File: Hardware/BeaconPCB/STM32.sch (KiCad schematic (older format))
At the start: 11 parts

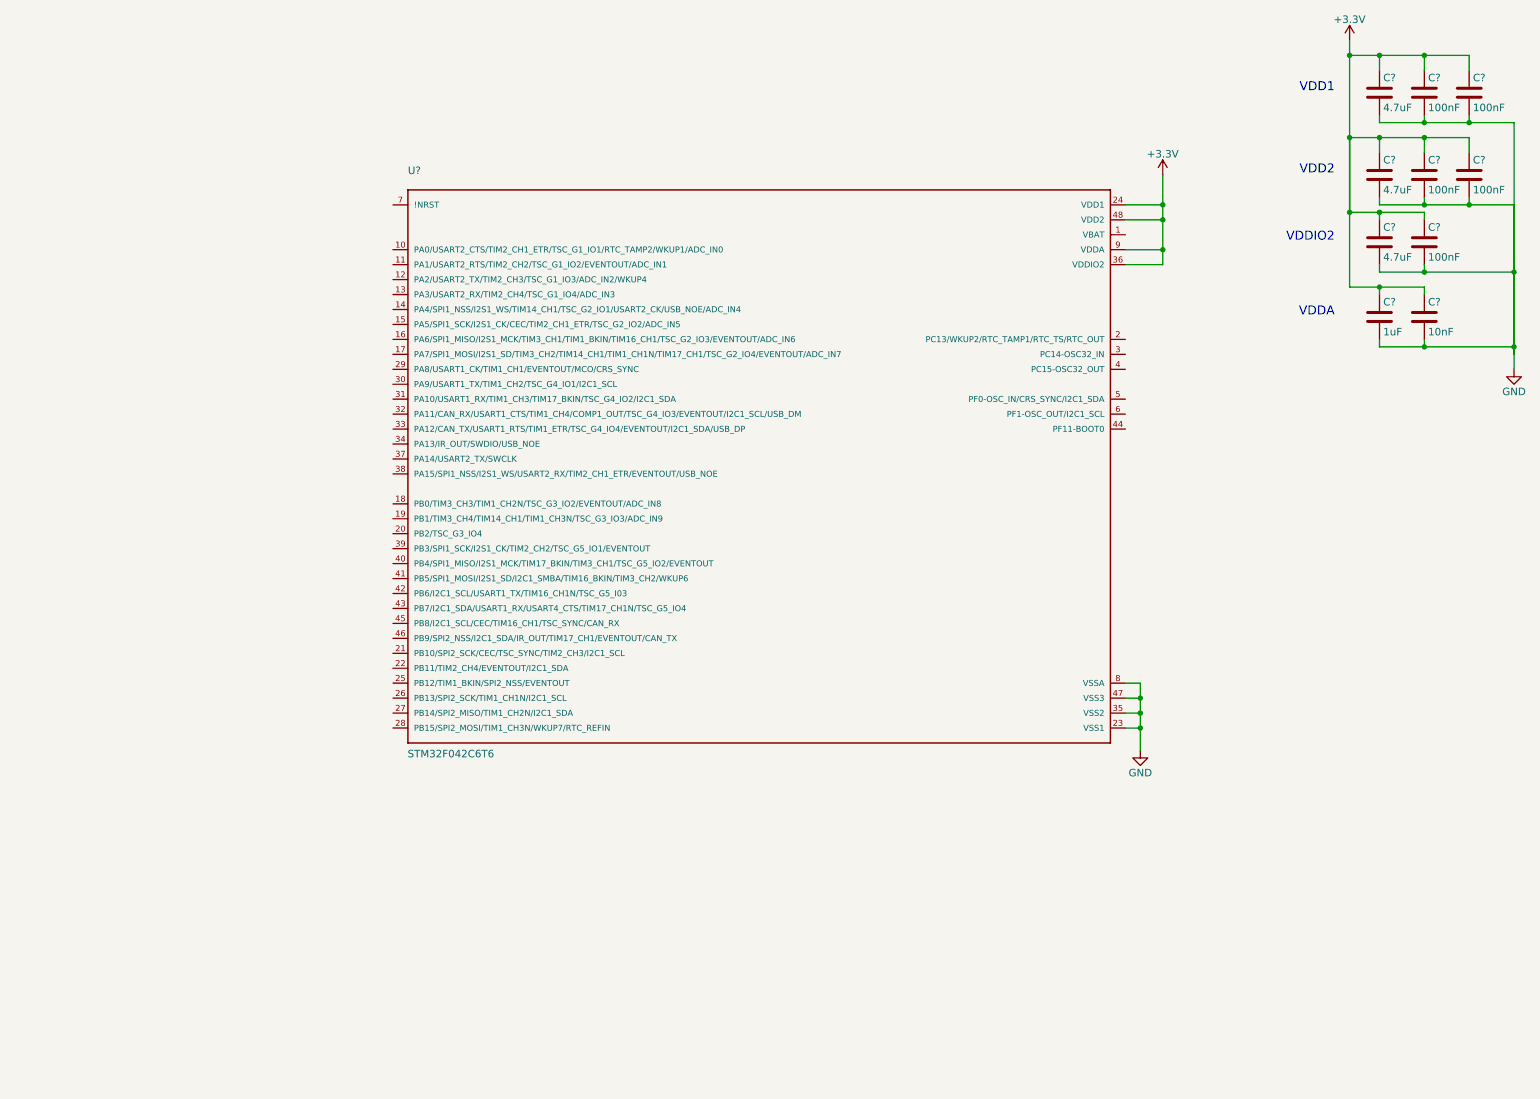
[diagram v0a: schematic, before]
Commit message: Base STM32 circuit schematic done
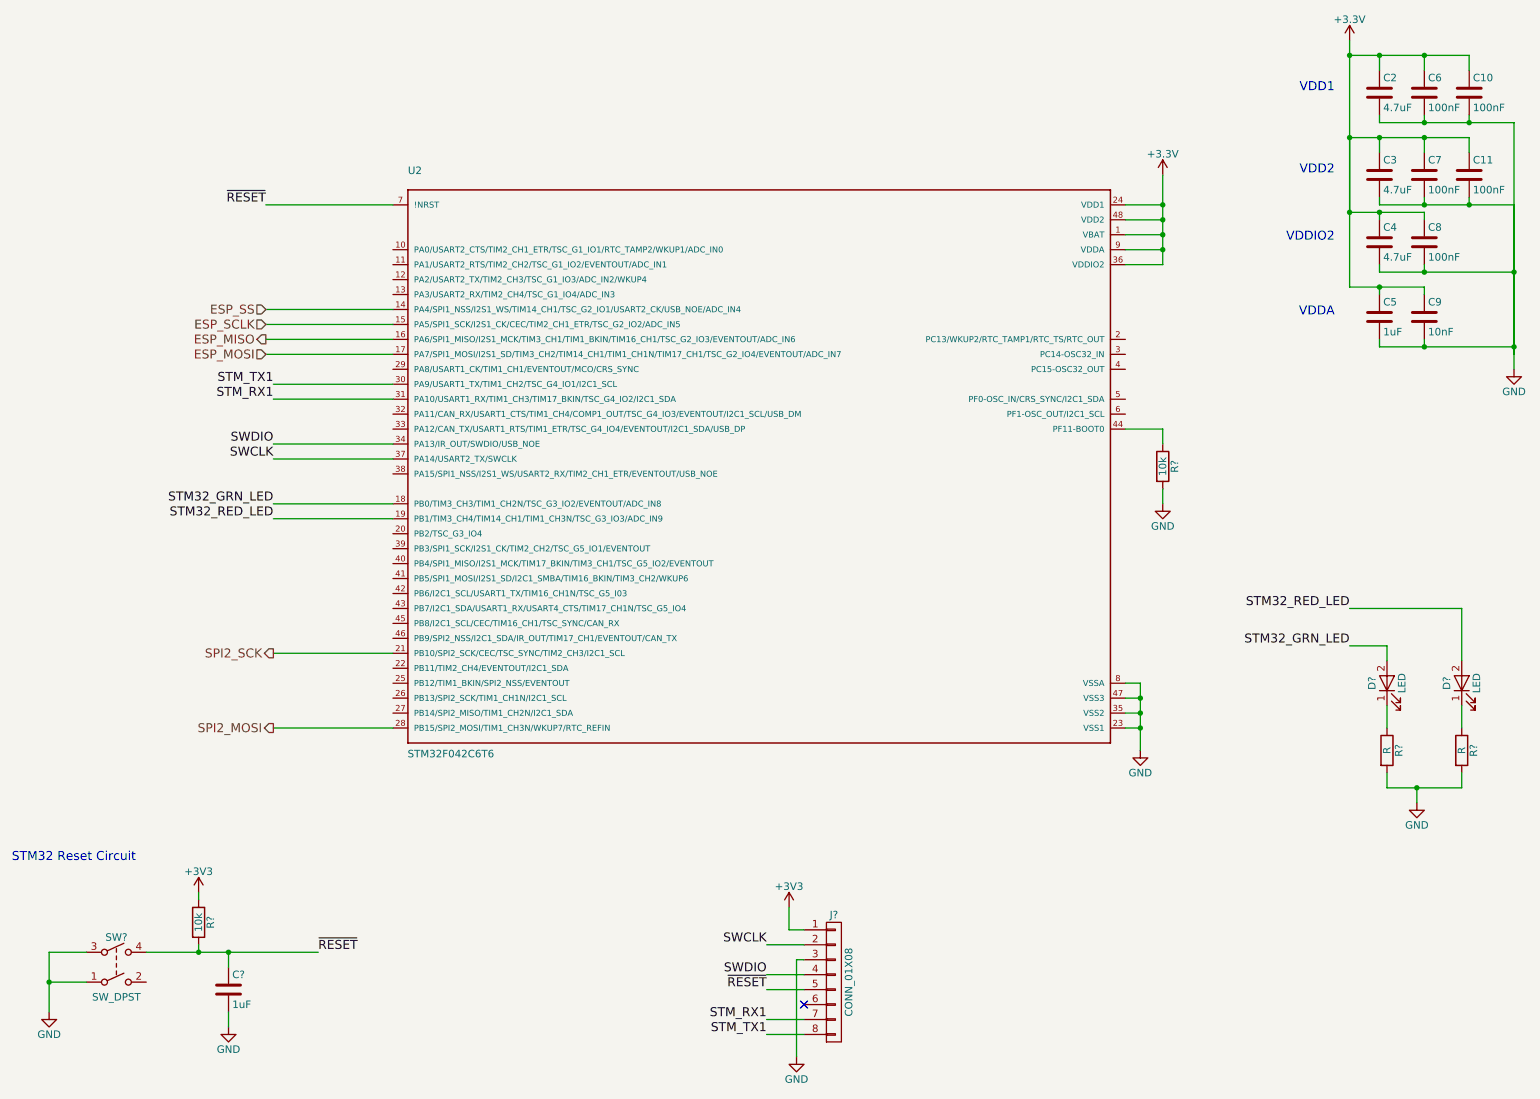
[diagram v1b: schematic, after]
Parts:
- added C?: 1uF, symbol C
- added D? (x2): LED, symbol LED
- added J?: CONN_01X08, symbol CONN_01X08
- added R? (x2): 10k, symbol R
- added R? (x2): R, symbol R
- added SW?: SW_DPST, symbol SW_DPST
- gave numbers to parts that had none: 11
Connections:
- net +3V3: now also U2.1 (VBAT), J?.1 (P1), R?.1
- net GND: now also C?.2, J?.3 (P3), R?.2, R?.2, R?.2, SW?.1, SW?.3
- net ESP_SS: now reaches U2.14 (PA4/SPI1_NSS/I2S1_WS/TIM14_CH1/TSC_G2_IO1/USART2_CK/USB_NOE/ADC_IN4)
- net ESP_SCLK: now reaches U2.15 (PA5/SPI1_SCK/I2S1_CK/CEC/TIM2_CH1_ETR/TSC_G2_IO2/ADC_IN5)
- net ESP_MISO: now reaches U2.16 (PA6/SPI1_MISO/I2S1_MCK/TIM3_CH1/TIM1_BKIN/TIM16_CH1/TSC_G2_IO3/EVENTOUT/ADC_IN6)
- net ESP_MOSI: now reaches U2.17 (PA7/SPI1_MOSI/I2S1_SD/TIM3_CH2/TIM14_CH1/TIM1_CH1N/TIM17_CH1/TSC_G2_IO4/EVENTOUT/ADC_IN7)
- net STM32_GRN_LED: now reaches U2.18 (PB0/TIM3_CH3/TIM1_CH2N/TSC_G3_IO2/EVENTOUT/ADC_IN8)
- net STM32_GRN_LED: now also D?.2 (A)
- net STM32_RED_LED: now reaches U2.19 (PB1/TIM3_CH4/TIM14_CH1/TIM1_CH3N/TSC_G3_IO3/ADC_IN9)
- net STM32_RED_LED: now also D?.2 (A)
- net SPI2_SCK: now reaches U2.21 (PB10/SPI2_SCK/CEC/TSC_SYNC/TIM2_CH3/I2C1_SCL)
- net SPI2_MOSI: now reaches U2.28 (PB15/SPI2_MOSI/TIM1_CH3N/WKUP7/RTC_REFIN)
- net STM_TX1: now reaches U2.30 (PA9/USART1_TX/TIM1_CH2/TSC_G4_IO1/I2C1_SCL)
- net STM_TX1: now also J?.8 (P8)
- net STM_RX1: now reaches U2.31 (PA10/USART1_RX/TIM1_CH3/TIM17_BKIN/TSC_G4_IO2/I2C1_SDA)
- net STM_RX1: now also J?.7 (P7)
- net SWDIO: now reaches U2.34 (PA13/IR_OUT/SWDIO/USB_NOE)
- net SWDIO: now also J?.4 (P4)
- net SWCLK: now reaches U2.37 (PA14/USART2_TX/SWCLK)
- net SWCLK: now also J?.2 (P2)
- net at U2.44 (PF11-BOOT0): now also R?.1
- net ~RESET: now reaches U2.7 (!NRST)
- net ~RESET: now also C?.1, J?.5 (P5), R?.2, SW?.4
- new net: D?.1 (K), R?.1 (x2)
- no-connect marks 0 -> 1
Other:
- note added: "STM32 Reset Circuit"

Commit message: Added IO buffers and APA102
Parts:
- added C? (x2): .1uF, symbol C
- added U? (x2): 74HC244, symbol 74HC244
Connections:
- net +3V3: now also C?.1, U?.20 (VCC)
- net ESP_MISO: now also U?.14 (1Y2); no longer U2.16 (PA6/SPI1_MISO/I2S1_MCK/TIM3_CH1/TIM1_BKIN/TIM16_CH1/TSC_G2_IO3/EVENTOUT/ADC_IN6)
- net ESP_MOSI: now also U?.8 (1A3); no longer U2.17 (PA7/SPI1_MOSI/I2S1_SD/TIM3_CH2/TIM14_CH1/TIM1_CH1N/TIM17_CH1/TSC_G2_IO4/EVENTOUT/ADC_IN7)
- net ESP_SCLK: now also U?.4 (1A1); no longer U2.15 (PA5/SPI1_SCK/I2S1_CK/CEC/TIM2_CH1_ETR/TSC_G2_IO2/ADC_IN5)
- net ESP_SS: now also U?.2 (1A0); no longer U2.14 (PA4/SPI1_NSS/I2S1_WS/TIM14_CH1/TSC_G2_IO1/USART2_CK/USB_NOE/ADC_IN4)
- net GND: now also C?.2, C?.2, U?.10 (GND), U?.10 (GND)
- net SPI2_MOSI: now also U?.16 (1Y1); no longer U2.28 (PB15/SPI2_MOSI/TIM1_CH3N/WKUP7/RTC_REFIN)
- net SPI2_SCK: now also U?.18 (1Y0); no longer U2.21 (PB10/SPI2_SCK/CEC/TSC_SYNC/TIM2_CH3/I2C1_SCL)
- net PORT0: now reaches U2.39 (PB3/SPI1_SCK/I2S1_CK/TIM2_CH2/TSC_G5_IO1/EVENTOUT)
- net PORT1: now reaches U2.40 (PB4/SPI1_MISO/I2S1_MCK/TIM17_BKIN/TIM3_CH1/TSC_G5_IO2/EVENTOUT)
- net PORT2: now reaches U2.41 (PB5/SPI1_MOSI/I2S1_SD/I2C1_SMBA/TIM16_BKIN/TIM3_CH2/WKUP6)
- net PORT3: now reaches U2.42 (PB6/I2C1_SCL/USART1_TX/TIM16_CH1N/TSC_G5_I03)
- net PORT4: now reaches U2.43 (PB7/I2C1_SDA/USART1_RX/USART4_CTS/TIM17_CH1N/TSC_G5_IO4)
- net PORT5: now reaches U2.45 (PB8/I2C1_SCL/CEC/TIM16_CH1/TSC_SYNC/CAN_RX)
- new net +5V: C?.1, U?.20 (VCC)
- new net SPI2_MOSI_LV: U2.28 (PB15/SPI2_MOSI/TIM1_CH3N/WKUP7/RTC_REFIN), U?.4 (1A1)
- new net SPI2_SCK_LV: U2.21 (PB10/SPI2_SCK/CEC/TSC_SYNC/TIM2_CH3/I2C1_SCL), U?.2 (1A0)
- new net STM32_MISO: U2.16 (PA6/SPI1_MISO/I2S1_MCK/TIM3_CH1/TIM1_BKIN/TIM16_CH1/TSC_G2_IO3/EVENTOUT/ADC_IN6)
- new net STM32_MOSI: U2.17 (PA7/SPI1_MOSI/I2S1_SD/TIM3_CH2/TIM14_CH1/TIM1_CH1N/TIM17_CH1/TSC_G2_IO4/EVENTOUT/ADC_IN7)
- new net STM32_SCLK: U2.15 (PA5/SPI1_SCK/I2S1_CK/CEC/TIM2_CH1_ETR/TSC_G2_IO2/ADC_IN5), U?.16 (1Y1)
- new net STM32_SS: U2.14 (PA4/SPI1_NSS/I2S1_WS/TIM14_CH1/TSC_G2_IO1/USART2_CK/USB_NOE/ADC_IN4), U?.18 (1Y0)
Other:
- moved on the sheet: C10, C11, C2, C3, C4, C5, C6, C7, C8, C9, C?, D?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

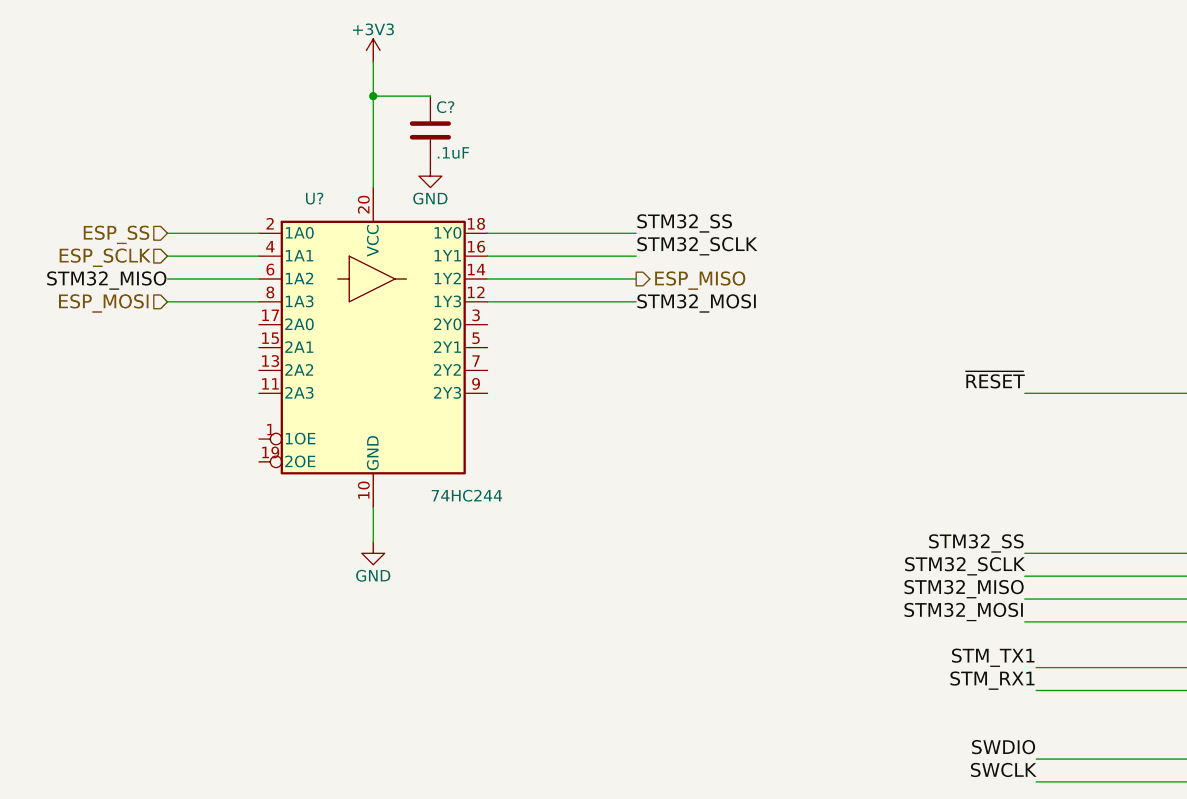
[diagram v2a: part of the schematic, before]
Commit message: Added Connectors Sheet
Started to re-arrange SPI lines
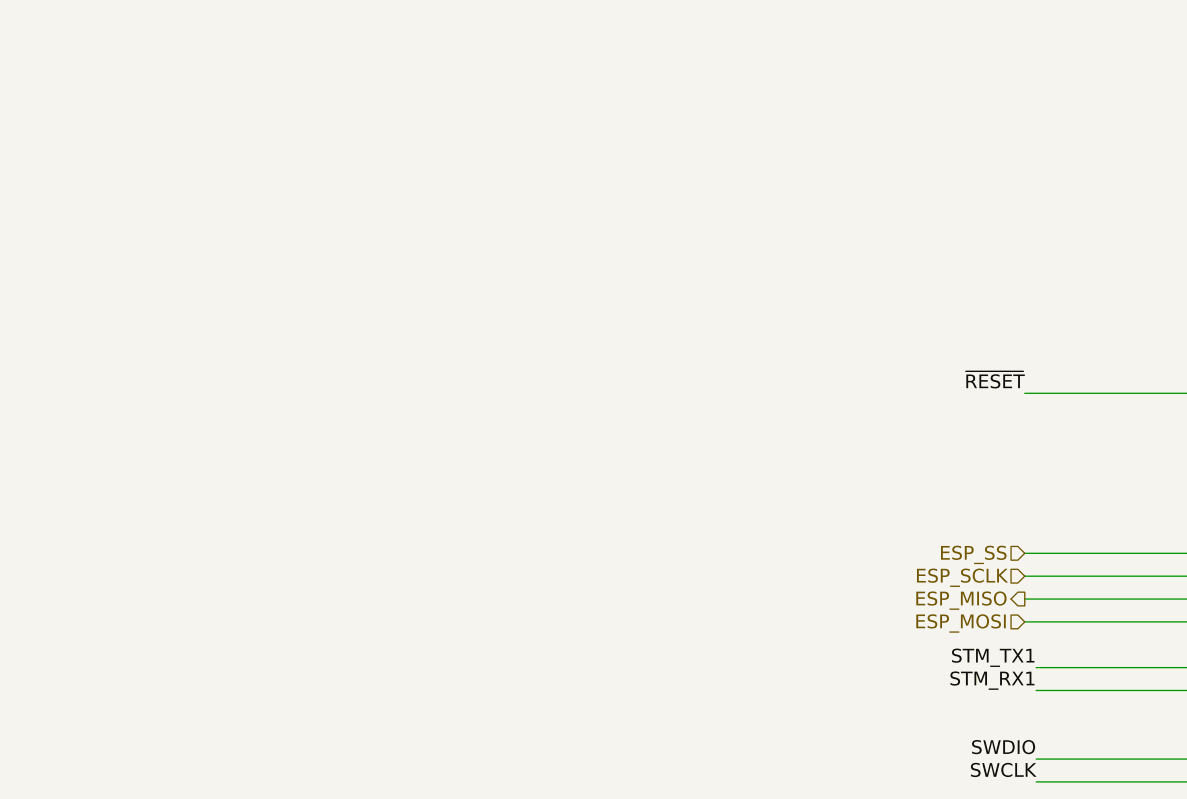
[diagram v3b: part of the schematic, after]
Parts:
- removed C?: .1uF, symbol C
- removed U?: 74HC244, symbol 74HC244
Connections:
- net STM32_MISO is gone; now on net ESP_MISO: U2.16 (PA6/SPI1_MISO/I2S1_MCK/TIM3_CH1/TIM1_BKIN/TIM16_CH1/TSC_G2_IO3/EVENTOUT/ADC_IN6)
- net STM32_MOSI is gone; now on net ESP_MOSI: U2.17 (PA7/SPI1_MOSI/I2S1_SD/TIM3_CH2/TIM14_CH1/TIM1_CH1N/TIM17_CH1/TSC_G2_IO4/EVENTOUT/ADC_IN7)
- net STM32_SCLK is gone; now on net ESP_SCLK: U2.15 (PA5/SPI1_SCK/I2S1_CK/CEC/TIM2_CH1_ETR/TSC_G2_IO2/ADC_IN5)
- net STM32_SS is gone; now on net ESP_SS: U2.14 (PA4/SPI1_NSS/I2S1_WS/TIM14_CH1/TSC_G2_IO1/USART2_CK/USB_NOE/ADC_IN4)
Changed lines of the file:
@@
 $Descr B 17000 11000
 encoding utf-8
-Sheet 3 5
+Sheet 3 6
 Title ""
 Date ""
@@
 	1    0    0    -1
 $EndComp
-Text HLabel 1800 1600 0    60   Input ~ 0
+Text HLabel 5550 3000 0    60   Input ~ 0
 ESP_SS
-Text HLabel 1800 1700 0    60   Input ~ 0
+Text HLabel 5550 3100 0    60   Input ~ 0
 ESP_SCLK
-Text HLabel 3850 1800 2    60   Output ~ 0
+Text HLabel 5550 3200 0    60   Output ~ 0
 ESP_MISO
-Text HLabel 1800 1900 0    60   Input ~ 0
+Text HLabel 5550 3300 0    60   Input ~ 0
 ESP_MOSI
 Text Label 5600 3900 2    60   ~ 0
@@
 	1    0    0    -1
 $EndComp
-$Comp
-L GND #PWR?
-U 1 1 59AECC3F
-P 2700 2950
-F 0 "#PWR?" H 2700 2700 50  0001 C CNN
-F 1 "GND" H 2700 2800 50  0000 C CNN
-F 2 "" H 2700 2950 50  0001 C CNN
-F 3 "" H 2700 2950 50  0001 C CNN
-	1    2700 2950
-	1    0    0    -1
-$EndComp
-$Comp
-L C C?
-U 1 1 59AECC45
-P 2950 1150
-F 0 "C?" H 2975 1250 50  0000 L CNN
-F 1 ".1uF" H 2975 1050 50  0000 L CNN
-F 2 "" H 2988 1000 50  0001 C CNN
-F 3 "" H 2950 1150 50  0001 C CNN
-	1    2950 1150
-	1    0    0    -1
-$EndComp
-$Comp
-L GND #PWR?
-U 1 1 59AECC4E
-P 2950 1300
-F 0 "#PWR?" H 2950 1050 50  0001 C CNN
-F 1 "GND" H 2950 1150 50  0000 C CNN
-F 2 "" H 2950 1300 50  0001 C CNN
-F 3 "" H 2950 1300 50  0001 C CNN
-	1    2950 1300
-	1    0    0    -1
-$EndComp
-$Comp
-L +3V3 #PWR?
-U 1 1 59AECCBA
-P 2700 850
-F 0 "#PWR?" H 2700 700 50  0001 C CNN
-F 1 "+3V3" H 2700 990 50  0000 C CNN
-F 2 "" H 2700 850 50  0001 C CNN
-F 3 "" H 2700 850 50  0001 C CNN
-	1    2700 850
-	1    0    0    -1
-$EndComp
-$Comp
-L 74HC244 U?
-U 1 1 59AECC33
-P 2700 2100
-F 0 "U?" H 2400 2750 50  0000 L CNN
-F 1 "74HC244" H 2950 1450 50  0000 L CNN
-F 2 "" H 2700 2100 50  0000 C CNN
-F 3 "" H 2700 2100 50  0000 C CNN
-	1    2700 2100
-	1    0    0    -1
-$EndComp
-Text Label 1800 1850 2    60   ~ 0
-STM32_MISO
-Text Label 3850 1700 0    60   ~ 0
-STM32_SCLK
-Text Label 3850 1950 0    60   ~ 0
-STM32_MOSI
-Text Label 5550 3100 2    60   ~ 0
-STM32_SCLK
-Text Label 5550 3200 2    60   ~ 0
-STM32_MISO
-Text Label 5550 3300 2    60   ~ 0
-STM32_MOSI
 Text HLabel 5600 4600 0    60   BiDi ~ 0
 PORT0
@@
 Text HLabel 5600 5100 0    60   BiDi ~ 0
 PORT5
-Text Label 3850 1600 0    60   ~ 0
-STM32_SS
-Text Label 5550 3000 2    60   ~ 0
-STM32_SS
-Wire Wire Line
-	1800 1900 2200 1900
-Wire Wire Line
-	1800 1700 2200 1700
-Wire Wire Line
-	1800 1600 2200 1600
-Wire Wire Line
-	2700 2950 2700 2800
-Connection ~ 2700 1000
-Wire Wire Line
-	2700 850  2700 1400
-Wire Wire Line
-	2950 1000 2700 1000
 Wire Wire Line
 	3050 7950 3050 7800
@@
 	14850 900  14850 2550
 Wire Wire Line
-	2200 1800 1800 1800
-Wire Wire Line
-	3200 1600 3850 1600
-Wire Wire Line
-	3200 1700 3850 1700
-Wire Wire Line
-	3200 1800 3850 1800
-Wire Wire Line
-	3200 1900 3850 1900
-Wire Wire Line
 	6400 4700 5600 4700

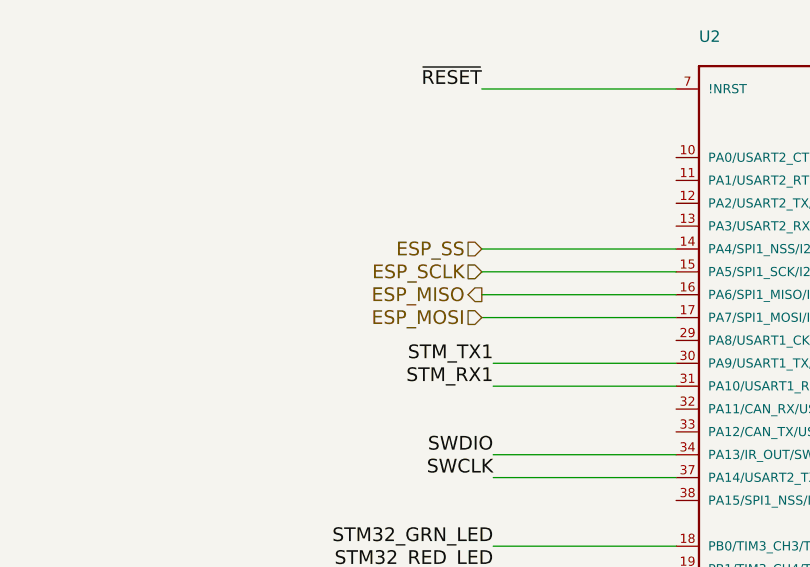
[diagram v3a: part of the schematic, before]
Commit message: Schematic Adjustments
Added 5V power line to Pi header
Adjusted the rest of schematic to use PI SPI lines
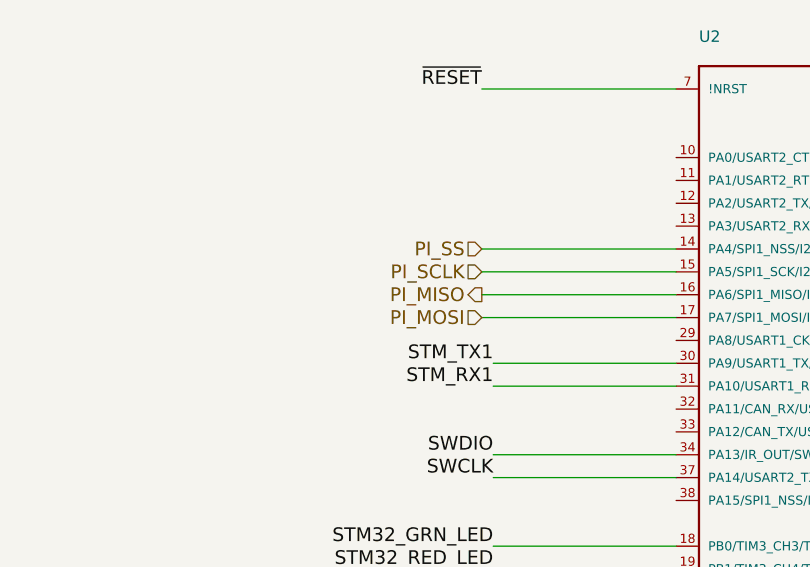
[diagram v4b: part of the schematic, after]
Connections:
- net ESP_MISO renamed PI_MISO
- net ESP_MOSI renamed PI_MOSI
- net ESP_SCLK renamed PI_SCLK
- net ESP_SS renamed PI_SS
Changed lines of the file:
@@
 $EndComp
 Text HLabel 5550 3000 0    60   Input ~ 0
-ESP_SS
+PI_SS
 Text HLabel 5550 3100 0    60   Input ~ 0
-ESP_SCLK
+PI_SCLK
 Text HLabel 5550 3200 0    60   Output ~ 0
-ESP_MISO
+PI_MISO
 Text HLabel 5550 3300 0    60   Input ~ 0
-ESP_MOSI
+PI_MOSI
 Text Label 5600 3900 2    60   ~ 0
 SWDIO
